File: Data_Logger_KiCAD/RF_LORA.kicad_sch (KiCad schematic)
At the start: 14 parts, among them U6 SX1262IMLTRT, U7 MASW-007221

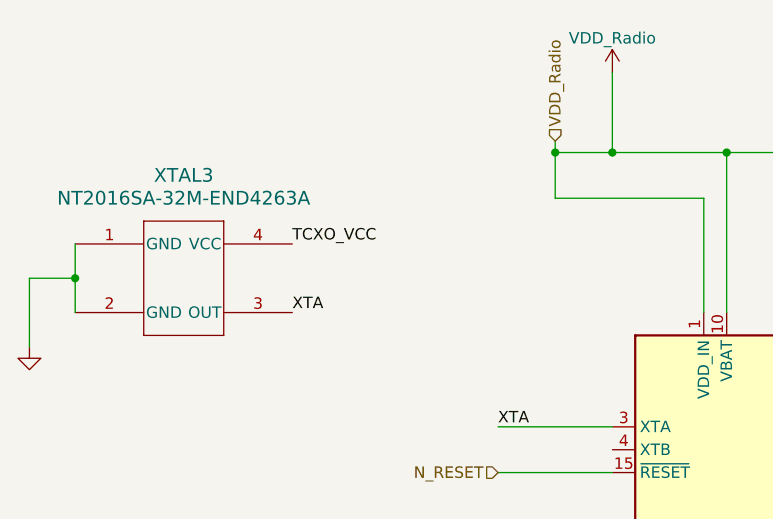
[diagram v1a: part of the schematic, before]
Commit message: Layout
Fixed via sizing, routed fanout from ESP
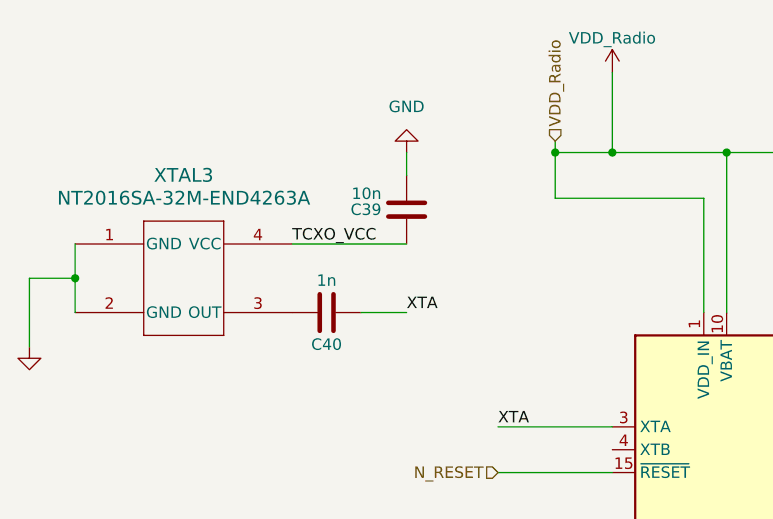
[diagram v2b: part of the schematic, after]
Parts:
- added C39: 10n, Capacitor_SMD:C_0402_1005Metric, symbol Device:C
- added C40: 1n, Capacitor_SMD:C_0402_1005Metric, symbol Device:C
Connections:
- net GND: now also C39.2
- net TCXO_VCC: now also C39.1
- net XTA: now also C40.2; no longer XTAL3.3 (OUT)
- new net: C40.1, XTAL3.3 (OUT)
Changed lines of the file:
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@@
+	(wire
+		(pts
+			(xy 60.96 40.64) (xy 60.96 38.1)
+		)
+		(stroke
+			(width 0)
+			(type default)
+		)
+	)
 	(wire
 		(pts
@@
 	(wire
 		(pts
+			(xy 55.88 55.88) (xy 60.96 55.88)
+		)
+		(stroke
+			(width 0)
+			(type default)
+		)
+	)
+	(wire
+		(pts
 			(xy 181.61 88.9) (xy 187.96 88.9)
 		)
@@
 		(pts
 			(xy 208.28 86.36) (xy 254 86.36)
+		)
+		(stroke
+			(width 0)
+			(type default)
+		)
+	)
+	(wire
+		(pts
+			(xy 48.26 48.26) (xy 60.96 48.26)
 		)
 		(stroke
@@
 		)
 	)
+	(label "XTA"
+		(at 60.96 55.88 0)
+		(effects
+			(font
+				(size 1.27 1.27)
+			)
+			(justify left bottom)
+		)
+	)
 	(label "DIO2"
 		(at 71.12 83.82 180)
@@
 			)
 			(justify right bottom)
-		)
-	)
-	(label "XTA"
-		(at 48.26 55.88 0)
-		(effects
-			(font
-				(size 1.27 1.27)
-			)
-			(justify left bottom)
 		)
 	)
@@
 	)
 	(symbol
+		(lib_id "Device:C")
+		(at 52.07 55.88 90)
+		(unit 1)
+		(exclude_from_sim no)
+		(in_bom yes)
+		(on_board yes)
+		(dnp no)
+		(property "Reference" "C40"
+			(at 52.07 59.436 90)
+			(effects
+				(font
+					(size 1.27 1.27)
+				)
+			)
+		)
+		(property "Value" "1n"
+			(at 52.07 52.324 90)
+			(effects
+				(font
+					(size 1.27 1.27)
+				)
+			)
+		)
+		(property "Footprint" "Capacitor_SMD:C_0402_1005Metric"
+			(at 55.88 54.9148 0)
+			(effects
+				(font
+					(size 1.27 1.27)
+				)
+				(hide yes)
+			)
+		)
+		(property "Datasheet" "~"
+			(at 52.07 55.88 0)
+			(effects
+				(font
+					(size 1.27 1.27)
+				)
+				(hide yes)
+			)
+		)
+		(property "Description" "Unpolarized capacitor"
+			(at 52.07 55.88 0)
+			(effects
+				(font
+					(size 1.27 1.27)
+				)
+				(hide yes)
+			)
+		)
+		(pin "2"
+		)
+		(pin "1"
+		)
+		(instances
+			(project "Data_Logger_Board"
+				(path "/db968e42-3ace-4cc9-9096-9d8f48135c40/795ab2be-9db7-4254-b05c-ac2b60177344/ddd17302-66df-4ba5-8c9c-bee0e050b0e0"
+					(reference "C40")
+					(unit 1)
+				)
+			)
+		)
+	)
+	(symbol
 		(lib_id "Device:R")
 		(at 196.85 129.54 90)
@@
 	)
 	(symbol
+		(lib_id "Device:C")
+		(at 60.96 44.45 180)
+		(unit 1)
+		(exclude_from_sim no)
+		(in_bom yes)
+		(on_board yes)
+		(dnp no)
+		(property "Reference" "C39"
+			(at 58.166 44.45 0)
+			(effects
+				(font
+					(size 1.27 1.27)
+				)
+				(justify left)
+			)
+		)
+		(property "Value" "10n"
+			(at 58.166 42.672 0)
+			(effects
+				(font
+					(size 1.27 1.27)
+				)
+				(justify left)
+			)
+		)
+		(property "Footprint" "Capacitor_SMD:C_0402_1005Metric"
+			(at 59.9948 40.64 0)
+			(effects
+				(font
+					(size 1.27 1.27)
+				)
+				(hide yes)
+			)
+		)
+		(property "Datasheet" "~"
+			(at 60.96 44.45 0)
+			(effects
+				(font
+					(size 1.27 1.27)
+				)
+				(hide yes)
+			)
+		)
+		(property "Description" "Unpolarized capacitor"
+			(at 60.96 44.45 0)
+			(effects
+				(font
+					(size 1.27 1.27)
+				)
+				(hide yes)
+			)
+		)
+		(pin "2"
+		)
+		(pin "1"
+		)
+		(instances
+			(project ""
+				(path "/db968e42-3ace-4cc9-9096-9d8f48135c40/795ab2be-9db7-4254-b05c-ac2b60177344/ddd17302-66df-4ba5-8c9c-bee0e050b0e0"
+					(reference "C39")
+					(unit 1)
+				)
+			)
+		)
+	)
+	(symbol
 		(lib_id "power:GND")
 		(at 157.48 101.6 0)
@@
 					(unit 1)
 				)
+			)
+		)
+	)
+	(symbol
+		(lib_id "power:GND")
+		(at 60.96 38.1 180)
+		(unit 1)
+		(exclude_from_sim no)
+		(in_bom yes)
+		(on_board yes)
+		(dnp no)
+		(fields_autoplaced yes)
+		(property "Reference" "#PWR073"
+			(at 60.96 31.75 0)
+			(effects
+				(font
+					(size 1.27 1.27)
+				)
+				(hide yes)
+			)
+		)
+		(property "Value" "GND"
+			(at 60.96 33.02 0)
+			(effects
+				(font
+					(size 1.27 1.27)
+				)
+			)
+		)
+		(property "Footprint" ""
+			(at 60.96 38.1 0)
+			(effects
+				(font
+					(size 1.27 1.27)
+				)
+				(hide yes)
+			)
+		)
+		(property "Datasheet" ""
+			(at 60.96 38.1 0)
+			(effects
+				(font
+					(size 1.27 1.27)
+				)
+				(hide yes)
+			)
+		)
+		(property "Description" "Power symbol creates a global label with name \"GND\" , ground"
+			(at 60.96 38.1 0)
+			(effects
+				(font
+					(size 1.27 1.27)
+				)
+				(hide yes)
+			)
+		)
+		(pin "1"
+		)
+		(instances
+			(project ""
+				(path "/db968e42-3ace-4cc9-9096-9d8f48135c40/795ab2be-9db7-4254-b05c-ac2b60177344/ddd17302-66df-4ba5-8c9c-bee0e050b0e0"
+					(reference "#PWR073")
+					(unit 1)
+				)

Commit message: save point
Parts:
- added FB1: FerriteBead_Small, Inductor_SMD:L_0603_1608Metric, symbol Device:FerriteBead_Small
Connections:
- net VDD_Radio: now also FB1.2; no longer U6.1 (VDD_IN), U6.10 (VBAT), U6.11 (VBAT_IO)
- new net: FB1.1, U6.1 (VDD_IN), U6.10 (VBAT), U6.11 (VBAT_IO)
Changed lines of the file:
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@@
 	(paper "A4")
+	(junction
+		(at 83.82 30.48)
+		(diameter 0)
+		(color 0 0 0 0)
+	)
 	(junction
 		(at 96.52 38.1)
@@
 	)
 	(junction
-		(at 104.14 38.1)
-		(diameter 0)
-		(color 0 0 0 0)
-	)
-	(junction
 		(at 203.2 113.03)
-		(diameter 0)
-		(color 0 0 0 0)
-	)
-	(junction
-		(at 77.47 38.1)
 		(diameter 0)
 		(color 0 0 0 0)
@@
 	(wire
 		(pts
-			(xy 83.82 29.21) (xy 83.82 38.1)
+			(xy 83.82 30.48) (xy 77.47 30.48)
+		)
+		(stroke
+			(width 0)
+			(type default)
+		)
+	)
+	(wire
+		(pts
+			(xy 83.82 29.21) (xy 83.82 30.48)
 		)
 		(stroke
@@
 	(wire
 		(pts
-			(xy 77.47 36.83) (xy 77.47 38.1)
-		)
-		(stroke
-			(width 0)
-			(type default)
-		)
-	)
-	(wire
-		(pts
 			(xy 62.23 101.6) (xy 83.82 101.6)
 		)
@@
 	(wire
 		(pts
+			(xy 77.47 27.94) (xy 77.47 30.48)
+		)
+		(stroke
+			(width 0)
+			(type default)
+		)
+	)
+	(wire
+		(pts
 			(xy 24.13 52.07) (xy 24.13 55.88)
 		)
@@
 	(wire
 		(pts
+			(xy 83.82 36.83) (xy 83.82 38.1)
+		)
+		(stroke
+			(width 0)
+			(type default)
+		)
+	)
+	(wire
+		(pts
 			(xy 130.81 63.5) (xy 133.35 63.5)
 		)
@@
 	(wire
 		(pts
-			(xy 104.14 38.1) (xy 111.76 38.1)
-		)
-		(stroke
-			(width 0)
-			(type default)
-		)
-	)
-	(wire
-		(pts
 			(xy 203.2 113.03) (xy 213.36 113.03)
 		)
@@
 	(wire
 		(pts
-			(xy 104.14 38.1) (xy 96.52 38.1)
-		)
-		(stroke
-			(width 0)
-			(type default)
-		)
-	)
-	(wire
-		(pts
 			(xy 120.65 69.85) (xy 120.65 71.12)
 		)
@@
 	(wire
 		(pts
-			(xy 96.52 38.1) (xy 83.82 38.1)
+			(xy 96.52 38.1) (xy 104.14 38.1)
 		)
 		(stroke
@@
 	(wire
 		(pts
+			(xy 111.76 30.48) (xy 111.76 39.37)
+		)
+		(stroke
+			(width 0)
+			(type default)
+		)
+	)
+	(wire
+		(pts
 			(xy 167.64 83.82) (xy 187.96 83.82)
 		)
@@
 	(wire
 		(pts
+			(xy 83.82 38.1) (xy 96.52 38.1)
+		)
+		(stroke
+			(width 0)
+			(type default)
+		)
+	)
+	(wire
+		(pts
 			(xy 120.65 69.85) (xy 132.08 69.85)
 		)
@@
 	(wire
 		(pts
-			(xy 111.76 38.1) (xy 111.76 39.37)
-		)
-		(stroke
-			(width 0)
-			(type default)
-		)
-	)
-	(wire
-		(pts
 			(xy 128.27 66.04) (xy 130.81 66.04)
 		)
@@
 		(pts
 			(xy 96.52 55.88) (xy 96.52 38.1)
+		)
+		(stroke
+			(width 0)
+			(type default)
+		)
+	)
+	(wire
+		(pts
+			(xy 83.82 30.48) (xy 111.76 30.48)
+		)
+		(stroke
+			(width 0)
+			(type default)
+		)
+	)
+	(wire
+		(pts
+			(xy 83.82 30.48) (xy 83.82 31.75)
 		)
 		(stroke
@@
 	(hierarchical_label "VDD_Radio"
 		(shape input)
-		(at 77.47 36.83 90)
+		(at 77.47 27.94 90)
 		(effects
 			(font
@@
 					(unit 1)
 				)
+			)
+		)
+	)
+	(symbol
+		(lib_id "Device:FerriteBead_Small")
+		(at 83.82 34.29 180)
+		(unit 1)
+		(exclude_from_sim no)
+		(in_bom yes)
+		(on_board yes)
+		(dnp no)
+		(property "Reference" "FB1"
+			(at 80.518 34.29 90)
+			(effects
+				(font
+					(size 1.27 1.27)
+				)
+			)
+		)
+		(property "Value" "FerriteBead_Small"
+			(at 80.01 34.3281 90)
+			(effects
+				(font
+					(size 1.27 1.27)
+				)
+				(hide yes)
+			)
+		)
+		(property "Footprint" "Inductor_SMD:L_0603_1608Metric"
+			(at 85.598 34.29 90)
+			(effects
+				(font
+					(size 1.27 1.27)
+				)
+				(hide yes)
+			)
+		)
+		(property "Datasheet" "~"
+			(at 83.82 34.29 0)
+			(effects
+				(font
+					(size 1.27 1.27)
+				)
+				(hide yes)
+			)
+		)
+		(property "Description" "Ferrite bead, small symbol"
+			(at 83.82 34.29 0)
+			(effects
+				(font
+					(size 1.27 1.27)
+				)
+				(hide yes)
+			)
+		)
+		(property "LCSC" " C14709"
+			(at 83.82 34.29 90)
+			(effects
+				(font
+					(size 1.27 1.27)
+				)
+				(hide yes)
+			)
+		)
+		(pin "2"
+		)
+		(pin "1"
+		)
+		(instances
+			(project "Data_Logger_Board"
+				(path "/db968e42-3ace-4cc9-9096-9d8f48135c40/795ab2be-9db7-4254-b05c-ac2b60177344/ddd17302-66df-4ba5-8c9c-bee0e050b0e0"
+					(reference "FB1")
+					(unit 1)
+				)

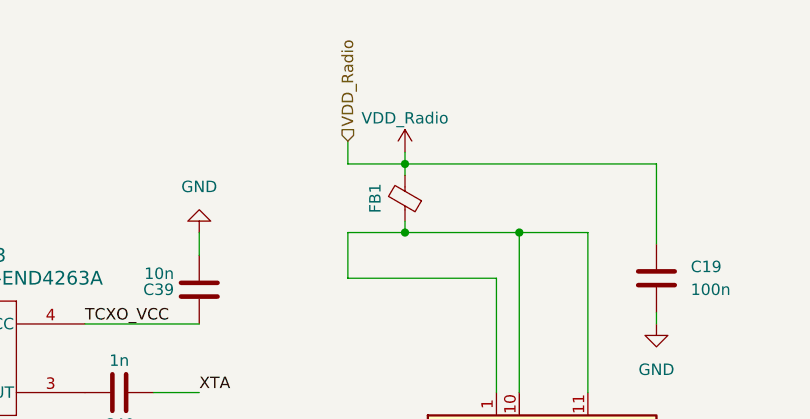
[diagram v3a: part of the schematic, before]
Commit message: layout power plane
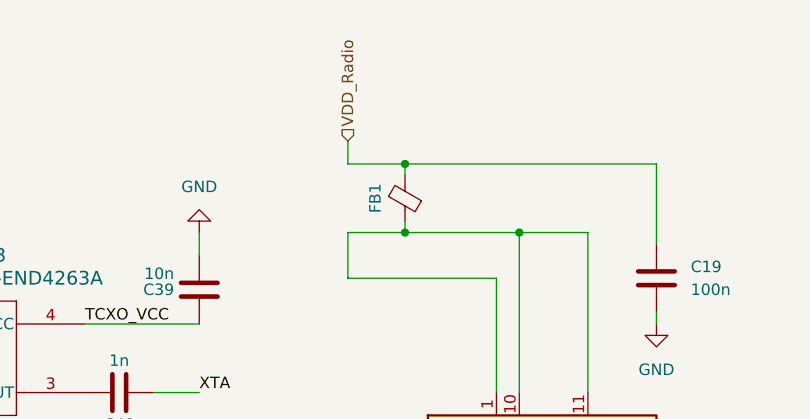
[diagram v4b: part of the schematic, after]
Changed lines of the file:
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@@
-	(wire
-		(pts
-			(xy 83.82 29.21) (xy 83.82 30.48)
-		)
-		(stroke
-			(width 0)
-			(type default)
-		)
-	)
 	(wire
 		(pts
@@
 					(unit 1)
 				)
-			)
-		)
-	)
-	(symbol
-		(lib_id "power:VDDA")
-		(at 83.82 29.21 0)
-		(unit 1)
-		(exclude_from_sim no)
-		(in_bom yes)
-		(on_board yes)
-		(dnp no)
-		(fields_autoplaced yes)
-		(property "Reference" "#PWR034"
-			(at 83.82 33.02 0)
-			(effects
-				(font
-					(size 1.27 1.27)
-				)
-				(hide yes)
-			)
-		)
-		(property "Value" "VDD_Radio"
-			(at 83.82 25.4 0)
-			(effects
-				(font
-					(size 1.27 1.27)
-				)
-			)
-		)
-		(property "Footprint" ""
-			(at 83.82 29.21 0)
-			(effects
-				(font
-					(size 1.27 1.27)
-				)
-				(hide yes)
-			)
-		)
-		(property "Datasheet" ""
-			(at 83.82 29.21 0)
-			(effects
-				(font
-					(size 1.27 1.27)
-				)
-				(hide yes)
-			)
-		)
-		(property "Description" "Power symbol creates a global label with name \"VDDA\""
-			(at 83.82 29.21 0)
-			(effects
-				(font
-					(size 1.27 1.27)
-				)
-				(hide yes)
-			)
-		)
-		(pin "1"
-		)
-		(instances
-			(project "RF_LORA"
-				(path "/8ae4759a-151c-407c-bd9a-b8440b531f27"
-					(reference "#PWR0101")
-					(unit 1)
-				)
-			)
-			(project ""
-				(path "/db968e42-3ace-4cc9-9096-9d8f48135c40/795ab2be-9db7-4254-b05c-ac2b60177344/ddd17302-66df-4ba5-8c9c-bee0e050b0e0"
-					(reference "#PWR034")
-					(unit 1)
-				)

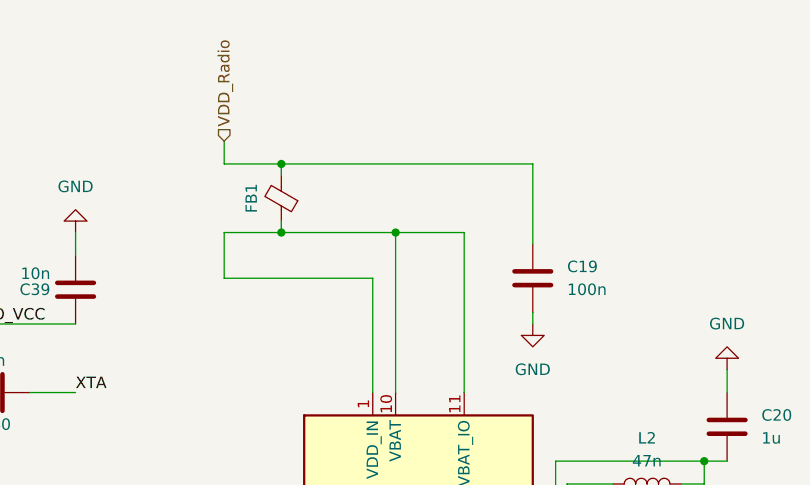
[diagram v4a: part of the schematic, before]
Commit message: layout
fix rf, usb netclass, add timepulse, round dimensions to even number, re-route GPS, 22 ohm in usb line, buttons to front, reg to front, change solder jumper for conn
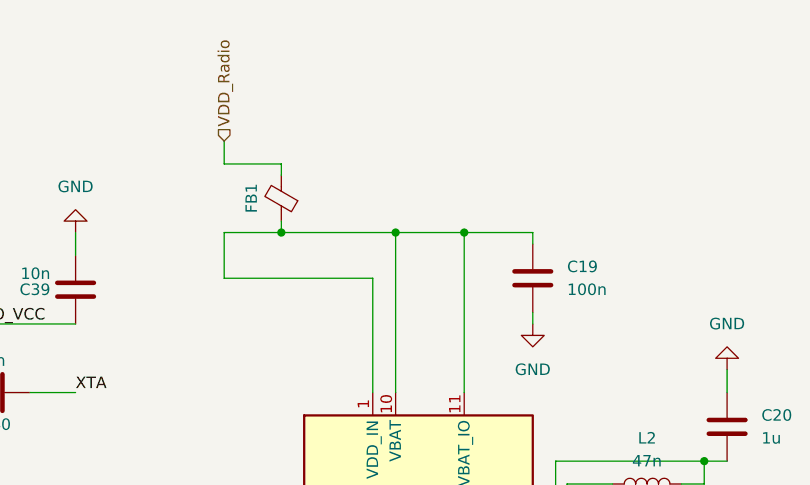
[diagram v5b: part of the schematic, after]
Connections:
- net VDD_Radio: no longer C19.1
- net at FB1.1, U6.1 (VDD_IN), U6.10 (VBAT)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: now also C19.1
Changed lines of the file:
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@@
 	(paper "A4")
-	(junction
-		(at 83.82 30.48)
-		(diameter 0)
-		(color 0 0 0 0)
-	)
 	(junction
 		(at 96.52 38.1)
@@
 	)
 	(junction
+		(at 104.14 38.1)
+		(diameter 0)
+		(color 0 0 0 0)
+	)
+	(junction
 		(at 203.2 129.54)
 		(diameter 0)
@@
 	(wire
 		(pts
+			(xy 104.14 38.1) (xy 111.76 38.1)
+		)
+		(stroke
+			(width 0)
+			(type default)
+		)
+	)
+	(wire
+		(pts
 			(xy 83.82 73.66) (xy 71.12 73.66)
 		)
@@
 	(wire
 		(pts
+			(xy 111.76 38.1) (xy 111.76 39.37)
+		)
+		(stroke
+			(width 0)
+			(type default)
+		)
+	)
+	(wire
+		(pts
 			(xy 19.05 52.07) (xy 19.05 59.69)
 		)
@@
 	(wire
 		(pts
-			(xy 111.76 30.48) (xy 111.76 39.37)
-		)
-		(stroke
-			(width 0)
-			(type default)
-		)
-	)
-	(wire
-		(pts
 			(xy 167.64 83.82) (xy 187.96 83.82)
 		)
@@
 		(pts
 			(xy 96.52 55.88) (xy 96.52 38.1)
-		)
-		(stroke
-			(width 0)
-			(type default)
-		)
-	)
-	(wire
-		(pts
-			(xy 83.82 30.48) (xy 111.76 30.48)
 		)
 		(stroke
@@
 		)
 	)
+	(netclass_flag ""
+		(length 2.54)
+		(shape round)
+		(at 121.92 83.82 0)
+		(fields_autoplaced yes)
+		(effects
+			(font
+				(size 1.27 1.27)
+			)
+			(justify left bottom)
+		)
+		(property "Netclass" "RF_50_SE"
+			(at 122.6185 81.28 0)
+			(effects
+				(font
+					(size 1.27 1.27)
+				)
+				(justify left)
+			)
+		)
+		(property "Component Class" ""
+			(at 50.8 13.97 0)
+			(effects
+				(font
+					(size 1.27 1.27)
+					(italic yes)
+				)
+			)
+		)
+	)
+	(netclass_flag ""
+		(length 2.54)
+		(shape round)
+		(at 173.99 83.82 0)
+		(fields_autoplaced yes)
+		(effects
+			(font
+				(size 1.27 1.27)
+			)
+			(justify left bottom)
+		)
+		(property "Netclass" "RF_50_SE"
+			(at 174.6885 81.28 0)
+			(effects
+				(font
+					(size 1.27 1.27)
+				)
+				(justify left)
+			)
+		)
+		(property "Component Class" ""
+			(at 100.33 13.97 0)
+			(effects
+				(font
+					(size 1.27 1.27)
+					(italic yes)
+				)
+			)
+		)
+	)
+	(netclass_flag ""
+		(length 2.54)
+		(shape round)
+		(at 223.52 86.36 0)
+		(fields_autoplaced yes)
+		(effects
+			(font
+				(size 1.27 1.27)
+			)
+			(justify left bottom)
+		)
+		(property "Netclass" "RF_50_SE"
+			(at 224.2185 83.82 0)
+			(effects
+				(font
+					(size 1.27 1.27)
+				)
+				(justify left)
+			)
+		)
+		(property "Component Class" ""
+			(at 87.63 17.78 0)
+			(effects
+				(font
+					(size 1.27 1.27)
+					(italic yes)
+				)
+			)
+		)
+	)

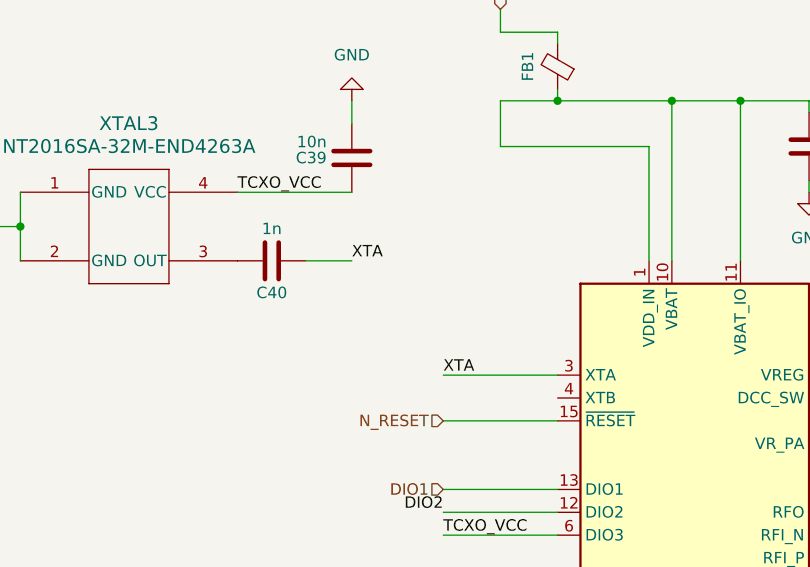
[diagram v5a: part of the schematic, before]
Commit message: Corrected DRC Errors
Added 220Ohm resistor to TCXO output.
Fixed DRC Errors
Added stitching vias
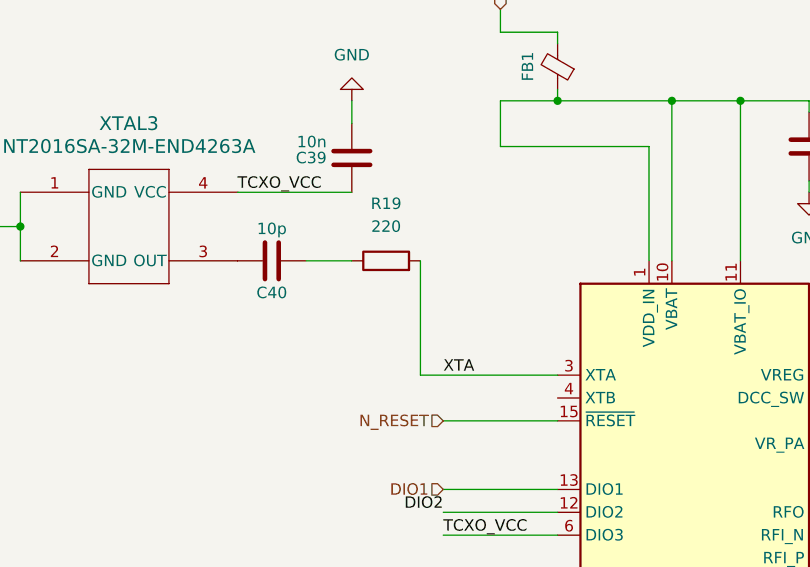
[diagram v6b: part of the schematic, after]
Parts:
- added R19: 220, Resistor_SMD:R_0402_1005Metric, symbol Device:R
- C40: value 1n -> 10p
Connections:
- net XTA: now also R19.2; no longer C40.2
- new net: C40.2, R19.1
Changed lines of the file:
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@@
-	(wire
-		(pts
-			(xy 71.12 68.58) (xy 83.82 68.58)
-		)
-		(stroke
-			(width 0)
-			(type default)
-		)
-	)
 	(wire
 		(pts
@@
 	(wire
 		(pts
+			(xy 68.58 55.88) (xy 68.58 68.58)
+		)
+		(stroke
+			(width 0)
+			(type default)
+		)
+	)
+	(wire
+		(pts
 			(xy 93.98 55.88) (xy 93.98 43.18)
 		)
@@
 		(pts
 			(xy 96.52 38.1) (xy 104.14 38.1)
+		)
+		(stroke
+			(width 0)
+			(type default)
+		)
+	)
+	(wire
+		(pts
+			(xy 68.58 68.58) (xy 83.82 68.58)
 		)
 		(stroke
@@
 	(label "TCXO_VCC"
 		(at 48.26 48.26 0)
-		(effects
-			(font
-				(size 1.27 1.27)
-			)
-			(justify left bottom)
-		)
-	)
-	(label "XTA"
-		(at 60.96 55.88 0)
 		(effects
 			(font
@@
 			)
 		)
-		(property "Value" "1n"
+		(property "Value" "10p"
 			(at 52.07 52.324 90)
 			(effects
@@
 					(unit 1)
 				)
+			)
+		)
+	)
+	(symbol
+		(lib_id "Device:R")
+		(at 64.77 55.88 90)
+		(unit 1)
+		(exclude_from_sim no)
+		(in_bom yes)
+		(on_board yes)
+		(dnp no)
+		(fields_autoplaced yes)
+		(property "Reference" "R19"
+			(at 64.77 49.53 90)
+			(effects
+				(font
+					(size 1.27 1.27)
+				)
+			)
+		)
+		(property "Value" "220"
+			(at 64.77 52.07 90)
+			(effects
+				(font
+					(size 1.27 1.27)
+				)
+			)
+		)
+		(property "Footprint" "Resistor_SMD:R_0402_1005Metric"
+			(at 64.77 57.658 90)
+			(effects
+				(font
+					(size 1.27 1.27)
+				)
+				(hide yes)
+			)
+		)
+		(property "Datasheet" "~"
+			(at 64.77 55.88 0)
+			(effects
+				(font
+					(size 1.27 1.27)
+				)
+				(hide yes)
+			)
+		)
+		(property "Description" "Resistor"
+			(at 64.77 55.88 0)
+			(effects
+				(font
+					(size 1.27 1.27)
+				)
+				(hide yes)
+			)
+		)
+		(pin "1"
+		)
+		(pin "2"
+		)
+		(instances
+			(project ""
+				(path "/db968e42-3ace-4cc9-9096-9d8f48135c40/795ab2be-9db7-4254-b05c-ac2b60177344/ddd17302-66df-4ba5-8c9c-bee0e050b0e0"
+					(reference "R19")
+					(unit 1)
+				)

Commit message: review LCSC fields
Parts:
- C39: LCSC (none) -> C15195
- C40: LCSC (none) -> C32949
- R19: LCSC (none) -> C25091
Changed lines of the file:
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@@
+			)
+		)
+		(property "LCSC" "C32949"
+			(at 52.07 55.88 90)
+			(effects
+				(font
+					(size 1.27 1.27)
+				)
+				(hide yes)
 			)
 		)
@@
 			)
 		)
+		(property "LCSC" "C15195"
+			(at 60.96 44.45 0)
+			(effects
+				(font
+					(size 1.27 1.27)
+				)
+				(hide yes)
+			)
+		)
 		(pin "2"
 		)
@@
 			(effects
 				(font
+					(size 1.27 1.27)
+				)
+				(hide yes)
+			)
+		)
+		(property "LCSC" "C25091"
+			(at 64.77 55.88 90)
+			(effects
+				(font

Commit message: schematic recs
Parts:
- XTAL3: LCSC (none) -> C36338880
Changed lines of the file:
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@@
+			)
+		)
+		(property "LCSC" "C36338880"
+			(at 15.24 50.8 0)
+			(effects
+				(font
+					(size 1.27 1.27)
+				)
+				(hide yes)
 			)
 		)
